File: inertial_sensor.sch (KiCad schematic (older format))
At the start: 6 parts

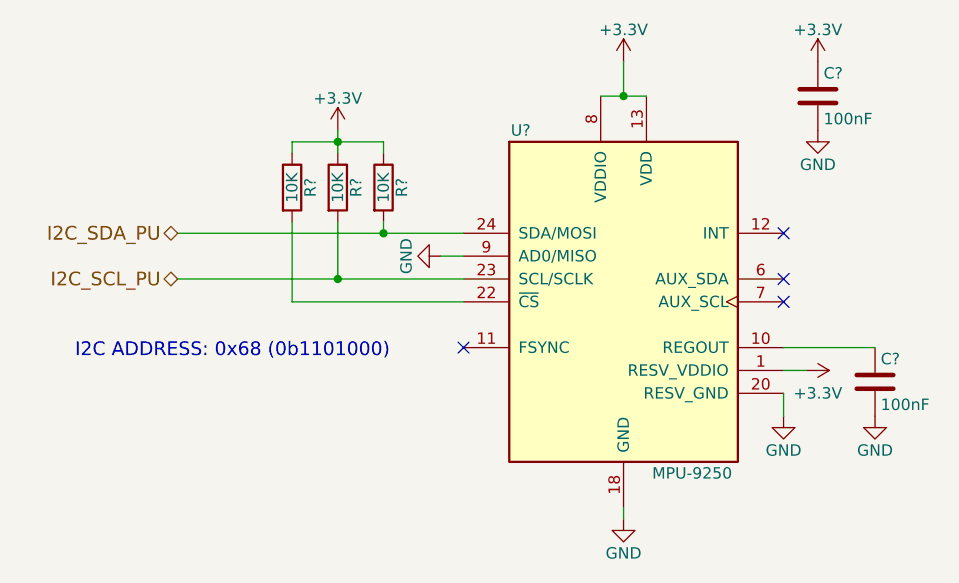
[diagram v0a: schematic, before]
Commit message: Make top-level connections between microcontroller and everything else
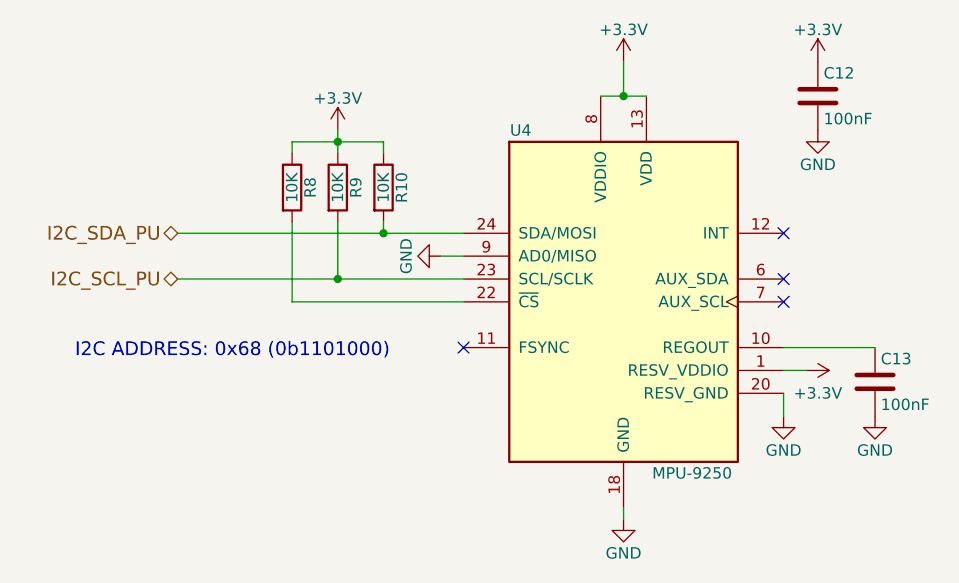
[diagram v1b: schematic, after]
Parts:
- gave numbers to parts that had none: 6
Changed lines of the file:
@@
 $EndDescr
 $Comp
-L MPU-9250 U?
+L MPU-9250 U4
 U 1 1 59A204FA
 P 5600 3300
-F 0 "U?" H 5150 4050 50  0000 C CNN
+F 0 "U4" H 5150 4050 50  0000 C CNN
 F 1 "MPU-9250" H 5900 2550 50  0000 C CNN
 F 2 "" H 5600 2300 50  0001 C CNN
@@
 Connection ~ 5600 2400
 $Comp
-L +3.3V #PWR?
+L +3.3V #PWR021
 U 1 1 59A206D2
 P 5600 2250
-F 0 "#PWR?" H 5600 2100 50  0001 C CNN
+F 0 "#PWR021" H 5600 2100 50  0001 C CNN
 F 1 "+3.3V" H 5600 2390 50  0000 C CNN
 F 2 "" H 5600 2250 50  0001 C CNN
@@
 $EndComp
 $Comp
-L GND #PWR?
+L GND #PWR022
 U 1 1 59A20700
 P 5600 4250
-F 0 "#PWR?" H 5600 4000 50  0001 C CNN
+F 0 "#PWR022" H 5600 4000 50  0001 C CNN
 F 1 "GND" H 5600 4100 50  0000 C CNN
 F 2 "" H 5600 4250 50  0001 C CNN
@@
 	5600 4250 5600 4200
 $Comp
-L GND #PWR?
+L GND #PWR023
 U 1 1 59A207DD
 P 4800 3100
-F 0 "#PWR?" H 4800 2850 50  0001 C CNN
+F 0 "#PWR023" H 4800 2850 50  0001 C CNN
 F 1 "GND" H 4800 2950 50  0000 C CNN
 F 2 "" H 4800 3100 50  0001 C CNN
@@
 $EndComp
 $Comp
-L C C?
+L C C13
 U 1 1 59A20809
 P 6700 3650
-F 0 "C?" H 6725 3750 50  0000 L CNN
+F 0 "C13" H 6725 3750 50  0000 L CNN
 F 1 "100nF" H 6725 3550 50  0000 L CNN
 F 2 "" H 6738 3500 50  0001 C CNN
@@
 	6700 3500 6300 3500
 $Comp
-L GND #PWR?
+L GND #PWR024
 U 1 1 59A20886
 P 6700 3800
-F 0 "#PWR?" H 6700 3550 50  0001 C CNN
+F 0 "#PWR024" H 6700 3550 50  0001 C CNN
 F 1 "GND" H 6700 3650 50  0000 C CNN
 F 2 "" H 6700 3800 50  0001 C CNN
@@
 $EndComp
 $Comp
-L R R?
+L R R10
 U 1 1 59A208DE
 P 4550 2800
-F 0 "R?" V 4630 2800 50  0000 C CNN
+F 0 "R10" V 4630 2800 50  0000 C CNN
 F 1 "10K" V 4550 2800 50  0000 C CNN
 F 2 "" V 4480 2800 50  0001 C CNN
@@
 $EndComp
 $Comp
-L R R?
+L R R9
 U 1 1 59A20952
 P 4350 2800
-F 0 "R?" V 4430 2800 50  0000 C CNN
+F 0 "R9" V 4430 2800 50  0000 C CNN
 F 1 "10K" V 4350 2800 50  0000 C CNN
 F 2 "" V 4280 2800 50  0001 C CNN
@@
 $EndComp
 $Comp
-L R R?
+L R R8
 U 1 1 59A20988
 P 4150 2800
-F 0 "R?" V 4230 2800 50  0000 C CNN
+F 0 "R8" V 4230 2800 50  0000 C CNN
 F 1 "10K" V 4150 2800 50  0000 C CNN
 F 2 "" V 4080 2800 50  0001 C CNN
@@
 Connection ~ 4350 2600
 $Comp
-L +3.3V #PWR?
+L +3.3V #PWR025
 U 1 1 59A20C50
 P 4350 2550
-F 0 "#PWR?" H 4350 2400 50  0001 C CNN
+F 0 "#PWR025" H 4350 2400 50  0001 C CNN
 F 1 "+3.3V" H 4350 2690 50  0000 C CNN
 F 2 "" H 4350 2550 50  0001 C CNN
@@
 NoConn ~ 6300 3000
 $Comp
-L +3.3V #PWR?
+L +3.3V #PWR026
 U 1 1 59A20EC2
 P 6450 2250
-F 0 "#PWR?" H 6450 2100 50  0001 C CNN
+F 0 "#PWR026" H 6450 2100 50  0001 C CNN
 F 1 "+3.3V" H 6450 2390 50  0000 C CNN
 F 2 "" H 6450 2250 50  0001 C CNN
@@
 $EndComp
 $Comp
-L C C?
+L C C12
 U 1 1 59A20EDC
 P 6450 2400
-F 0 "C?" H 6475 2500 50  0000 L CNN
+F 0 "C12" H 6475 2500 50  0000 L CNN
 F 1 "100nF" H 6475 2300 50  0000 L CNN
 F 2 "" H 6488 2250 50  0001 C CNN
@@
 $EndComp
 $Comp
-L GND #PWR?
+L GND #PWR027
 U 1 1 59A20F44
 P 6450 2550
-F 0 "#PWR?" H 6450 2300 50  0001 C CNN
+F 0 "#PWR027" H 6450 2300 50  0001 C CNN
 F 1 "GND" H 6450 2400 50  0000 C CNN
 F 2 "" H 6450 2550 50  0001 C CNN
@@
 $EndComp
 $Comp
-L GND #PWR?
+L GND #PWR028
 U 1 1 59A212F4
 P 6300 3800
-F 0 "#PWR?" H 6300 3550 50  0001 C CNN
+F 0 "#PWR028" H 6300 3550 50  0001 C CNN
 F 1 "GND" H 6300 3650 50  0000 C CNN
 F 2 "" H 6300 3800 50  0001 C CNN
@@
 $EndComp
 $Comp
-L +3.3V #PWR?
+L +3.3V #PWR029
 U 1 1 59A2134D
 P 6400 3600
-F 0 "#PWR?" H 6400 3450 50  0001 C CNN
+F 0 "#PWR029" H 6400 3450 50  0001 C CNN
 F 1 "+3.3V" V 6500 3650 50  0000 C CNN
 F 2 "" H 6400 3600 50  0001 C CNN

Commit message: Assigned some footprints and added CR1225 holder footprint
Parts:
- C12, C13: footprint (none) -> Capacitors_SMD:C_0603
- R10, R8, R9: footprint (none) -> Resistors_SMD:R_0603
- U4: footprint (none) -> Housings_DFN_QFN:QFN-24-1EP_3x3mm_Pitch0.4mm
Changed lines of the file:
@@
 F 0 "U4" H 5150 4050 50  0000 C CNN
 F 1 "MPU-9250" H 5900 2550 50  0000 C CNN
-F 2 "" H 5600 2300 50  0001 C CNN
+F 2 "Housings_DFN_QFN:QFN-24-1EP_3x3mm_Pitch0.4mm" H 5600 2300 50  0001 C CNN
 F 3 "" H 5600 3150 50  0001 C CNN
 	1    5600 3300
@@
 F 0 "C13" H 6725 3750 50  0000 L CNN
 F 1 "100nF" H 6725 3550 50  0000 L CNN
-F 2 "" H 6738 3500 50  0001 C CNN
+F 2 "Capacitors_SMD:C_0603" H 6738 3500 50  0001 C CNN
 F 3 "" H 6700 3650 50  0001 C CNN
 	1    6700 3650
@@
 F 0 "R10" V 4630 2800 50  0000 C CNN
 F 1 "10K" V 4550 2800 50  0000 C CNN
-F 2 "" V 4480 2800 50  0001 C CNN
+F 2 "Resistors_SMD:R_0603" V 4480 2800 50  0001 C CNN
 F 3 "" H 4550 2800 50  0001 C CNN
 	1    4550 2800
@@
 F 0 "R9" V 4430 2800 50  0000 C CNN
 F 1 "10K" V 4350 2800 50  0000 C CNN
-F 2 "" V 4280 2800 50  0001 C CNN
+F 2 "Resistors_SMD:R_0603" V 4280 2800 50  0001 C CNN
 F 3 "" H 4350 2800 50  0001 C CNN
 	1    4350 2800
@@
 F 0 "R8" V 4230 2800 50  0000 C CNN
 F 1 "10K" V 4150 2800 50  0000 C CNN
-F 2 "" V 4080 2800 50  0001 C CNN
+F 2 "Resistors_SMD:R_0603" V 4080 2800 50  0001 C CNN
 F 3 "" H 4150 2800 50  0001 C CNN
 	1    4150 2800
@@
 F 0 "C12" H 6475 2500 50  0000 L CNN
 F 1 "100nF" H 6475 2300 50  0000 L CNN
-F 2 "" H 6488 2250 50  0001 C CNN
+F 2 "Capacitors_SMD:C_0603" H 6488 2250 50  0001 C CNN
 F 3 "" H 6450 2400 50  0001 C CNN
 	1    6450 2400

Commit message: Create relevant BOM links, export digikey BOM
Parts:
- U4: MFR (none) -> TDK InvenSense; MPN (none) -> MPU-9250; SPN (none) -> 1428-1019-1-ND; SPR (none) -> https://www.digikey.com.au/
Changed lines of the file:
@@
 U 1 1 59A204FA
 P 5600 3300
-F 0 "U4" H 5150 4050 50  0000 C CNN
-F 1 "MPU-9250" H 5900 2550 50  0000 C CNN
-F 2 "Housings_DFN_QFN:QFN-24-1EP_3x3mm_Pitch0.4mm" H 5600 2300 50  0001 C CNN
-F 3 "" H 5600 3150 50  0001 C CNN
+F 0 "U4" H 5150 4050 50 0000 C CNN
+F 1 "MPU-9250" H 5900 2550 50 0000 C CNN
+F 2 "Housings_DFN_QFN:QFN-24-1EP_3x3mm_Pitch0.4mm" H 5600 2300 50 0001 C CNN
+F 3 "http://store.invensense.com/datasheets/invensense/MPU9250REV1.0.pdf" H 5600 3150 50 0001 C CNN
+F 4 "TDK InvenSense" H 0 0 50 0001 C CNN "MFR"
+F 5 "MPU-9250" H 0 0 50 0001 C CNN "MPN"
+F 6 "https://www.digikey.com.au/" H 0 0 50 0001 C CNN "SPR"
+F 7 "1428-1019-1-ND" H 0 0 50 0001 C CNN "SPN"
+F 8 "" H 0 0 50 0001 C CNN "SPURL"
 	1    5600 3300
 	1    0    0    -1
 $EndComp
-Wire Wire Line
-	5700 2400 5500 2400
-Wire Wire Line
-	5600 2400 5600 2250
-Connection ~ 5600 2400
 $Comp
 L +3.3V #PWR021
 U 1 1 59A206D2
 P 5600 2250
-F 0 "#PWR021" H 5600 2100 50  0001 C CNN
-F 1 "+3.3V" H 5600 2390 50  0000 C CNN
-F 2 "" H 5600 2250 50  0001 C CNN
-F 3 "" H 5600 2250 50  0001 C CNN
+F 0 "#PWR021" H 5600 2100 50 0001 C CNN
+F 1 "+3.3V" H 5600 2390 50 0000 C CNN
+F 2 "" H 5600 2250 50 0001 C CNN
+F 3 "" H 5600 2250 50 0001 C CNN
 	1    5600 2250
 	1    0    0    -1
@@
 U 1 1 59A20700
 P 5600 4250
-F 0 "#PWR022" H 5600 4000 50  0001 C CNN
-F 1 "GND" H 5600 4100 50  0000 C CNN
-F 2 "" H 5600 4250 50  0001 C CNN
-F 3 "" H 5600 4250 50  0001 C CNN
+F 0 "#PWR022" H 5600 4000 50 0001 C CNN
+F 1 "GND" H 5600 4100 50 0000 C CNN
+F 2 "" H 5600 4250 50 0001 C CNN
+F 3 "" H 5600 4250 50 0001 C CNN
 	1    5600 4250
 	1    0    0    -1
 $EndComp
-Wire Wire Line
-	5600 4250 5600 4200
 $Comp
 L GND #PWR023
 U 1 1 59A207DD
 P 4800 3100
-F 0 "#PWR023" H 4800 2850 50  0001 C CNN
-F 1 "GND" H 4800 2950 50  0000 C CNN
-F 2 "" H 4800 3100 50  0001 C CNN
-F 3 "" H 4800 3100 50  0001 C CNN
+F 0 "#PWR023" H 4800 2850 50 0001 C CNN
+F 1 "GND" H 4800 2950 50 0000 C CNN
+F 2 "" H 4800 3100 50 0001 C CNN
+F 3 "" H 4800 3100 50 0001 C CNN
 	1    4800 3100
 	0    1    1    0
@@
 U 1 1 59A20809
 P 6700 3650
-F 0 "C13" H 6725 3750 50  0000 L CNN
-F 1 "100nF" H 6725 3550 50  0000 L CNN
-F 2 "Capacitors_SMD:C_0603" H 6738 3500 50  0001 C CNN
-F 3 "" H 6700 3650 50  0001 C CNN
+F 0 "C13" H 6725 3750 50 0000 L CNN
+F 1 "100nF" H 6725 3550 50 0000 L CNN
+F 2 "Capacitors_SMD:C_0603" H 6738 3500 50 0001 C CNN
+F 3 "" H 6700 3650 50 0001 C CNN
+F 4 "" H 0 0 50 0001 C CNN "MFR"
+F 5 "" H 0 0 50 0001 C CNN "MPN"
+F 6 "" H 0 0 50 0001 C CNN "SPR"
+F 7 "" H 0 0 50 0001 C CNN "SPN"
+F 8 "" H 0 0 50 0001 C CNN "SPURL"
 	1    6700 3650
 	1    0    0    -1
 $EndComp
-Wire Wire Line
-	6700 3500 6300 3500
 $Comp
 L GND #PWR024
 U 1 1 59A20886
 P 6700 3800
-F 0 "#PWR024" H 6700 3550 50  0001 C CNN
-F 1 "GND" H 6700 3650 50  0000 C CNN
-F 2 "" H 6700 3800 50  0001 C CNN
-F 3 "" H 6700 3800 50  0001 C CNN
+F 0 "#PWR024" H 6700 3550 50 0001 C CNN
+F 1 "GND" H 6700 3650 50 0000 C CNN
+F 2 "" H 6700 3800 50 0001 C CNN
+F 3 "" H 6700 3800 50 0001 C CNN
 	1    6700 3800
 	1    0    0    -1
@@
 U 1 1 59A208DE
 P 4550 2800
-F 0 "R10" V 4630 2800 50  0000 C CNN
-F 1 "10K" V 4550 2800 50  0000 C CNN
-F 2 "Resistors_SMD:R_0603" V 4480 2800 50  0001 C CNN
-F 3 "" H 4550 2800 50  0001 C CNN
+F 0 "R10" V 4630 2800 50 0000 C CNN
+F 1 "10K" V 4550 2800 50 0000 C CNN
+F 2 "Resistors_SMD:R_0603" V 4480 2800 50 0001 C CNN
+F 3 "" H 4550 2800 50 0001 C CNN
+F 4 "" H 0 0 50 0001 C CNN "MFR"
+F 5 "" H 0 0 50 0001 C CNN "MPN"
+F 6 "" H 0 0 50 0001 C CNN "SPR"
+F 7 "" H 0 0 50 0001 C CNN "SPN"
+F 8 "" H 0 0 50 0001 C CNN "SPURL"
 	1    4550 2800
 	1    0    0    -1
@@
 U 1 1 59A20952
 P 4350 2800
-F 0 "R9" V 4430 2800 50  0000 C CNN
-F 1 "10K" V 4350 2800 50  0000 C CNN
-F 2 "Resistors_SMD:R_0603" V 4280 2800 50  0001 C CNN
-F 3 "" H 4350 2800 50  0001 C CNN
+F 0 "R9" V 4430 2800 50 0000 C CNN
+F 1 "10K" V 4350 2800 50 0000 C CNN
+F 2 "Resistors_SMD:R_0603" V 4280 2800 50 0001 C CNN
+F 3 "" H 4350 2800 50 0001 C CNN
+F 4 "" H 0 0 50 0001 C CNN "MFR"
+F 5 "" H 0 0 50 0001 C CNN "MPN"
+F 6 "" H 0 0 50 0001 C CNN "SPR"
+F 7 "" H 0 0 50 0001 C CNN "SPN"
+F 8 "" H 0 0 50 0001 C CNN "SPURL"
 	1    4350 2800
 	1    0    0    -1
@@
 U 1 1 59A20988
 P 4150 2800
-F 0 "R8" V 4230 2800 50  0000 C CNN
-F 1 "10K" V 4150 2800 50  0000 C CNN
-F 2 "Resistors_SMD:R_0603" V 4080 2800 50  0001 C CNN
-F 3 "" H 4150 2800 50  0001 C CNN
+F 0 "R8" V 4230 2800 50 0000 C CNN
+F 1 "10K" V 4150 2800 50 0000 C CNN
+F 2 "Resistors_SMD:R_0603" V 4080 2800 50 0001 C CNN
+F 3 "" H 4150 2800 50 0001 C CNN
+F 4 "" H 0 0 50 0001 C CNN "MFR"
+F 5 "" H 0 0 50 0001 C CNN "MPN"
+F 6 "" H 0 0 50 0001 C CNN "SPR"
+F 7 "" H 0 0 50 0001 C CNN "SPN"
+F 8 "" H 0 0 50 0001 C CNN "SPURL"
 	1    4150 2800
 	1    0    0    -1
 $EndComp
-Wire Wire Line
-	4150 3300 4900 3300
-Wire Wire Line
-	3650 3200 4900 3200
-Wire Wire Line
-	3650 3000 4900 3000
-Wire Wire Line
-	4900 3100 4800 3100
-Wire Wire Line
-	4150 3300 4150 2950
-Wire Wire Line
-	4350 3200 4350 2950
-Wire Wire Line
-	4550 3000 4550 2950
-Wire Wire Line
-	4550 2650 4550 2600
-Wire Wire Line
-	4550 2600 4150 2600
-Wire Wire Line
-	4150 2600 4150 2650
-Wire Wire Line
-	4350 2550 4350 2650
-Connection ~ 4350 2600
 $Comp
 L +3.3V #PWR025
 U 1 1 59A20C50
 P 4350 2550
-F 0 "#PWR025" H 4350 2400 50  0001 C CNN
-F 1 "+3.3V" H 4350 2690 50  0000 C CNN
-F 2 "" H 4350 2550 50  0001 C CNN
-F 3 "" H 4350 2550 50  0001 C CNN
+F 0 "#PWR025" H 4350 2400 50 0001 C CNN
+F 1 "+3.3V" H 4350 2690 50 0000 C CNN
+F 2 "" H 4350 2550 50 0001 C CNN
+F 3 "" H 4350 2550 50 0001 C CNN
 	1    4350 2550
 	1    0    0    -1
 $EndComp
-NoConn ~ 4900 3500
-NoConn ~ 6300 3200
-NoConn ~ 6300 3300
-NoConn ~ 6300 3000
 $Comp
 L +3.3V #PWR026
 U 1 1 59A20EC2
 P 6450 2250
-F 0 "#PWR026" H 6450 2100 50  0001 C CNN
-F 1 "+3.3V" H 6450 2390 50  0000 C CNN
-F 2 "" H 6450 2250 50  0001 C CNN
-F 3 "" H 6450 2250 50  0001 C CNN
+F 0 "#PWR026" H 6450 2100 50 0001 C CNN
+F 1 "+3.3V" H 6450 2390 50 0000 C CNN
+F 2 "" H 6450 2250 50 0001 C CNN
+F 3 "" H 6450 2250 50 0001 C CNN
 	1    6450 2250
 	1    0    0    -1
@@
 U 1 1 59A20EDC
 P 6450 2400
-F 0 "C12" H 6475 2500 50  0000 L CNN
-F 1 "100nF" H 6475 2300 50  0000 L CNN
-F 2 "Capacitors_SMD:C_0603" H 6488 2250 50  0001 C CNN
-F 3 "" H 6450 2400 50  0001 C CNN
+F 0 "C12" H 6475 2500 50 0000 L CNN
+F 1 "100nF" H 6475 2300 50 0000 L CNN
+F 2 "Capacitors_SMD:C_0603" H 6488 2250 50 0001 C CNN
+F 3 "" H 6450 2400 50 0001 C CNN
+F 4 "" H 0 0 50 0001 C CNN "MFR"
+F 5 "" H 0 0 50 0001 C CNN "MPN"
+F 6 "" H 0 0 50 0001 C CNN "SPR"
+F 7 "" H 0 0 50 0001 C CNN "SPN"
+F 8 "" H 0 0 50 0001 C CNN "SPURL"
 	1    6450 2400
 	1    0    0    -1
@@
 U 1 1 59A20F44
 P 6450 2550
-F 0 "#PWR027" H 6450 2300 50  0001 C CNN
-F 1 "GND" H 6450 2400 50  0000 C CNN
-F 2 "" H 6450 2550 50  0001 C CNN
-F 3 "" H 6450 2550 50  0001 C CNN
+F 0 "#PWR027" H 6450 2300 50 0001 C CNN
+F 1 "GND" H 6450 2400 50 0000 C CNN
+F 2 "" H 6450 2550 50 0001 C CNN
+F 3 "" H 6450 2550 50 0001 C CNN
 	1    6450 2550
 	1    0    0    -1
@@
 U 1 1 59A212F4
 P 6300 3800
-F 0 "#PWR028" H 6300 3550 50  0001 C CNN
-F 1 "GND" H 6300 3650 50  0000 C CNN
-F 2 "" H 6300 3800 50  0001 C CNN
-F 3 "" H 6300 3800 50  0001 C CNN
+F 0 "#PWR028" H 6300 3550 50 0001 C CNN
+F 1 "GND" H 6300 3650 50 0000 C CNN
+F 2 "" H 6300 3800 50 0001 C CNN
+F 3 "" H 6300 3800 50 0001 C CNN
 	1    6300 3800
 	1    0    0    -1
@@
 U 1 1 59A2134D
 P 6400 3600
-F 0 "#PWR029" H 6400 3450 50  0001 C CNN
-F 1 "+3.3V" V 6500 3650 50  0000 C CNN
-F 2 "" H 6400 3600 50  0001 C CNN
-F 3 "" H 6400 3600 50  0001 C CNN
+F 0 "#PWR029" H 6400 3450 50 0001 C CNN
+F 1 "+3.3V" V 6500 3650 50 0000 C CNN
+F 2 "" H 6400 3600 50 0001 C CNN
+F 3 "" H 6400 3600 50 0001 C CNN
 	1    6400 3600
 	0    1    1    0
 $EndComp
-Wire Wire Line
-	6400 3600 6300 3600
-Wire Wire Line
-	6300 3700 6300 3800
-Connection ~ 4350 3200
-Connection ~ 4550 3000
 Text HLabel 3650 3000 0    60   BiDi ~ 0
 I2C_SDA_PU
@@
 Text Notes 3200 3550 0    60   ~ 0
 I2C ADDRESS: 0x68 (0b1101000)
+Wire Wire Line
+	5700 2400 5500 2400
+Wire Wire Line
+	5600 2400 5600 2250
+Wire Wire Line
+	5600 4250 5600 4200
+Wire Wire Line
+	6700 3500 6300 3500
+Wire Wire Line
+	4150 3300 4900 3300
+Wire Wire Line
+	3650 3200 4900 3200
+Wire Wire Line
+	3650 3000 4900 3000
+Wire Wire Line
+	4900 3100 4800 3100
+Wire Wire Line
+	4150 3300 4150 2950
+Wire Wire Line
+	4350 3200 4350 2950
+Wire Wire Line
+	4550 3000 4550 2950
+Wire Wire Line
+	4550 2650 4550 2600
+Wire Wire Line
+	4550 2600 4150 2600
+Wire Wire Line
+	4150 2600 4150 2650
+Wire Wire Line
+	4350 2550 4350 2650
+Wire Wire Line
+	6400 3600 6300 3600
+Wire Wire Line
+	6300 3700 6300 3800
+Connection ~ 5600 2400
+Connection ~ 4350 2600
+Connection ~ 4350 3200
+Connection ~ 4550 3000
+NoConn ~ 4900 3500
+NoConn ~ 6300 3200
+NoConn ~ 6300 3300
+NoConn ~ 6300 3000
 $EndSCHEMATC
